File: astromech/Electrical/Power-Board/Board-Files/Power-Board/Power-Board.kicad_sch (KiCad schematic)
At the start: 20 parts

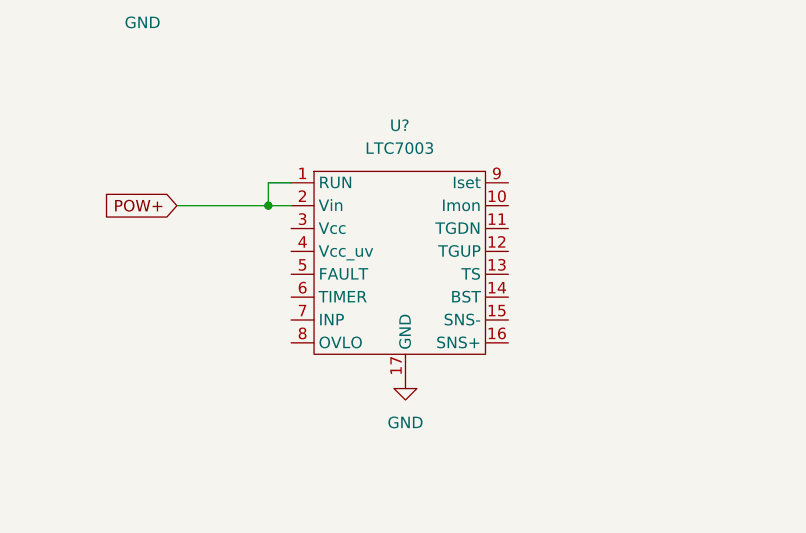
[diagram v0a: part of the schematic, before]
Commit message: Updated LTC7003 symbol
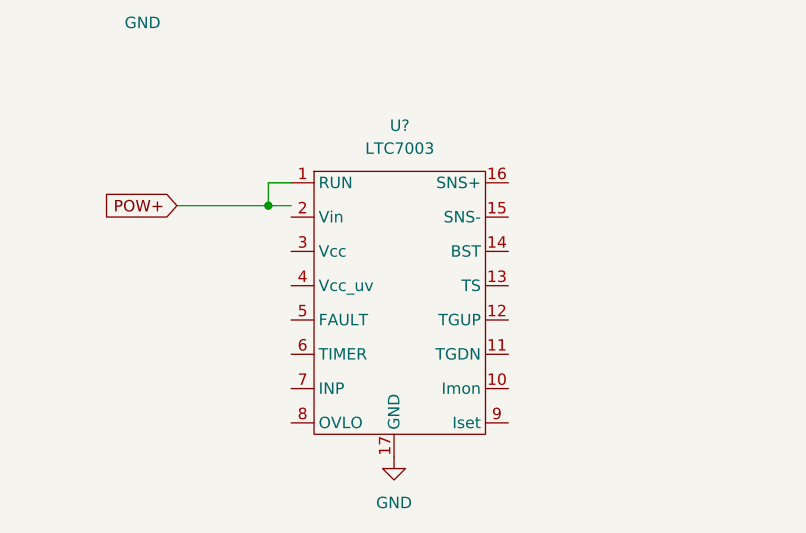
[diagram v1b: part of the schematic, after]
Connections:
- net POW+: no longer U?.2 (Vin)
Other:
- moved on the sheet: U?
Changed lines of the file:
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@@
     (pin "1")
   )
-  (symbol (lib_id "power:GND") (at 115.57 143.51 0) (unit 1)
-    (in_bom yes) (on_board yes) (fields_autoplaced)
-    (property "Reference" "#PWR?" (id 0) (at 115.57 149.86 0)
-      (effects (font (size 1.27 1.27)) hide)
-    )
-    (property "Value" "GND" (id 1) (at 115.57 148.59 0))
-    (property "Footprint" "" (id 2) (at 115.57 143.51 0)
-      (effects (font (size 1.27 1.27)) hide)
-    )
-    (property "Datasheet" "" (id 3) (at 115.57 143.51 0)
+  (symbol (lib_id "power:GND") (at 114.3 152.4 0) (unit 1)
+    (in_bom yes) (on_board yes) (fields_autoplaced)
+    (property "Reference" "#PWR?" (id 0) (at 114.3 158.75 0)
+      (effects (font (size 1.27 1.27)) hide)
+    )
+    (property "Value" "GND" (id 1) (at 114.3 157.48 0))
+    (property "Footprint" "" (id 2) (at 114.3 152.4 0)
+      (effects (font (size 1.27 1.27)) hide)
+    )
+    (property "Datasheet" "" (id 3) (at 114.3 152.4 0)
       (effects (font (size 1.27 1.27)) hide)
     )
@@
       (effects (font (size 1.27 1.27)) hide)
     )
-    (property "Datasheet" "" (id 3) (at 107.95 127 0)
-      (effects (font (size 1.27 1.27)) hide)
-    )
+    (property "Datasheet" "" (id 3) (at 107.95 129.54 0)
+      (effects (font (size 1.27 1.27)) hide)
+    )

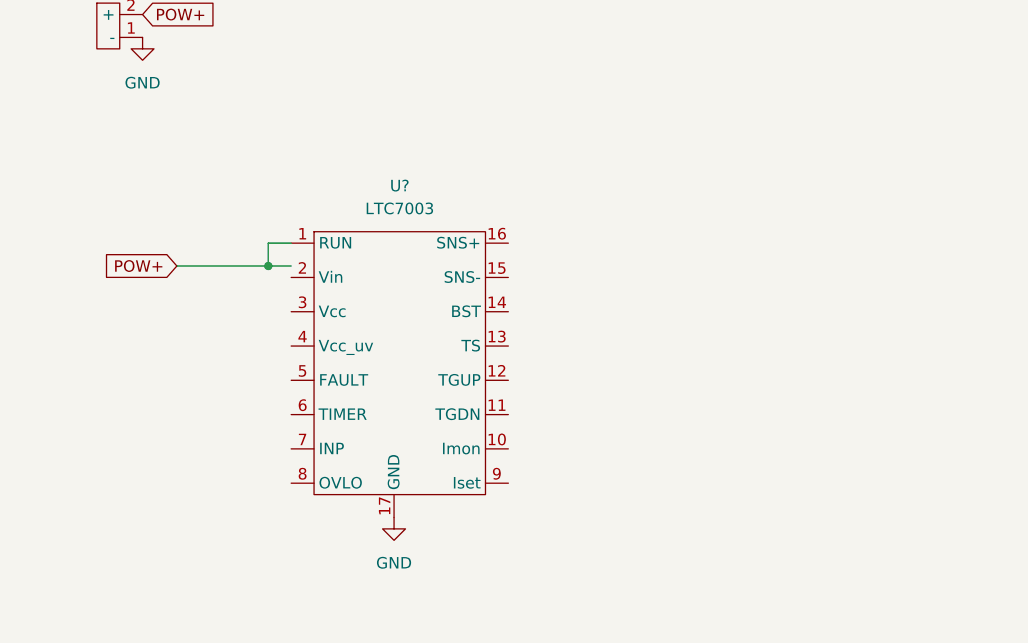
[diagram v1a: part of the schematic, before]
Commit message: added main switch LTC7003
Generic symbols used. Not many symbols have associated footprints
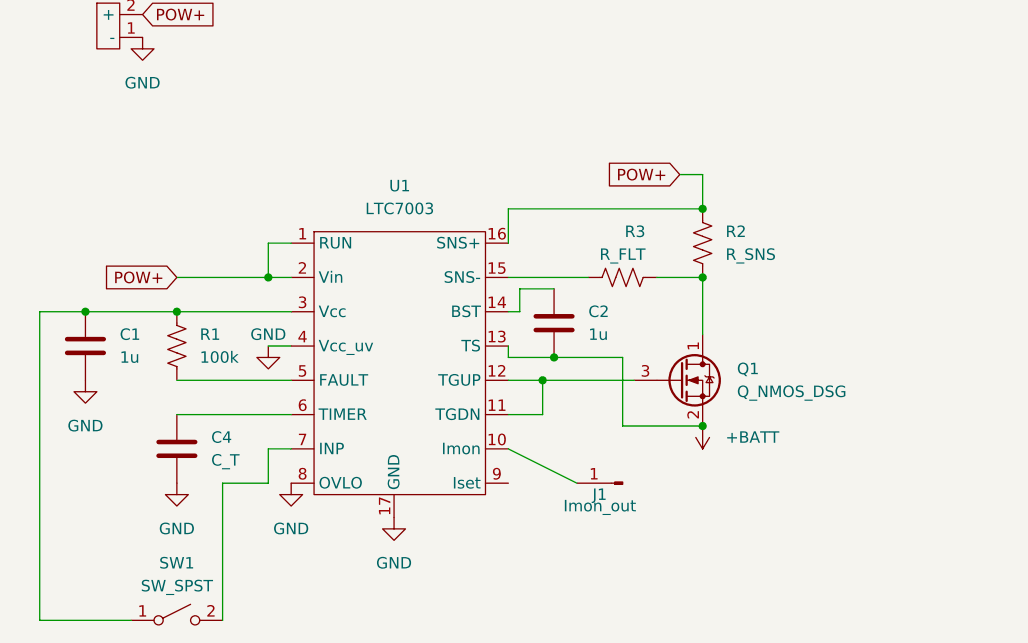
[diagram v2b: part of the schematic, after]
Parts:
- added C1, C2: 1u, symbol Device:C
- added C4: C_T, symbol Device:C
- added J1: Imon_out, symbol Connector:Conn_01x01_Male
- added Q1: Q_NMOS_DSG, symbol Device:Q_NMOS_DSG
- added R1: 100k, symbol Device:R_US
- added R2: R_SNS, symbol Device:R_US
- added R3: R_FLT, symbol Device:R_US
- added SW1: SW_SPST, symbol Switch:SW_SPST
- gave numbers to parts that had none: 1
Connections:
- net +BATT: now also U1.13 (TS), C2.2, Q1.2 (S)
- net GND: now also U1.4 (Vcc_uv), U1.8 (OVLO), C1.2, C4.2
- net POW+: now also U1.16 (SNS+), U1.2 (Vin), R2.1
- net at U1.10 (Imon): now also J1.1 (Pin_1)
- net at U1.11 (TGDN): now also U1.12 (TGUP), Q1.3 (G)
- net at U1.14 (BST): now also C2.1
- net at U1.15 (SNS-): now also R3.1
- net at U1.3 (Vcc): now also C1.1, R1.1, SW1.1 (A)
- net at U1.5 (FAULT): now also R1.2
- net at U1.6 (TIMER): now also C4.1
- net at U1.7 (INP): now also SW1.2 (B)
- new net: Q1.1 (D), R2.2, R3.2

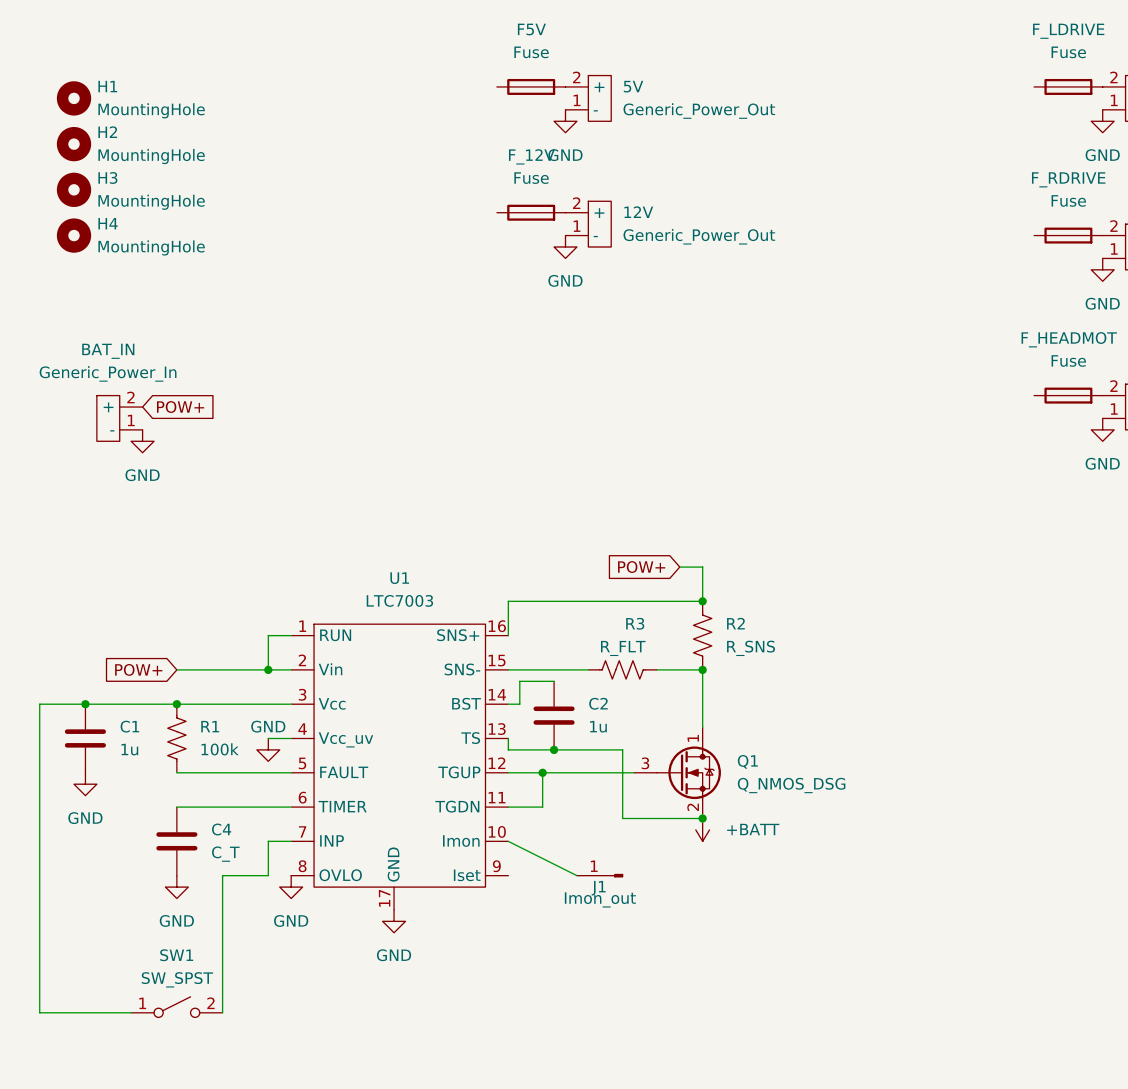
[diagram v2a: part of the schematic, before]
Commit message: Added 5v Regulator
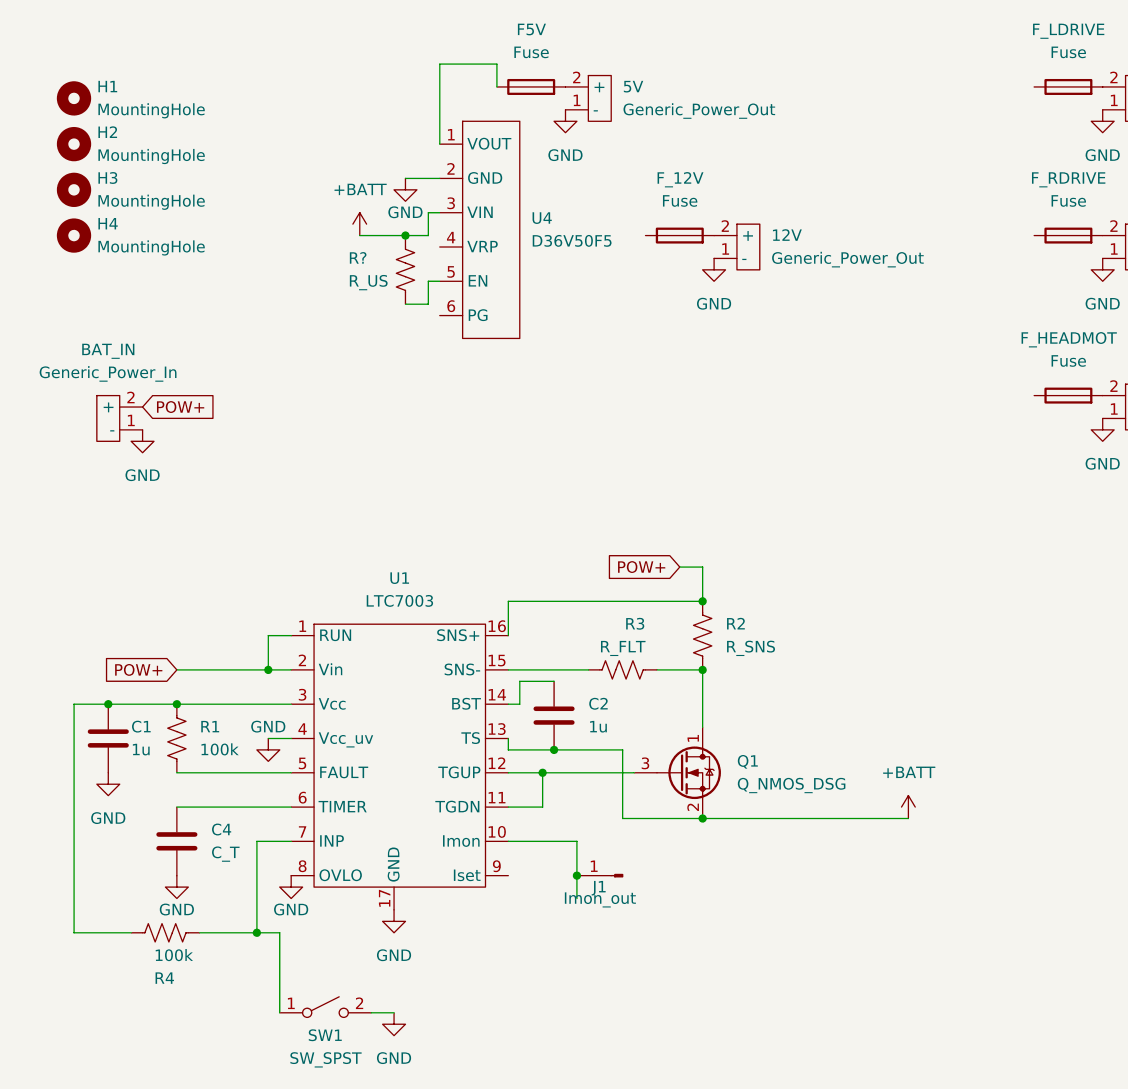
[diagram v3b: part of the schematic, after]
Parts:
- added R4: 100k, symbol Device:R_US
- added R?: R_US, symbol Device:R_US
- added U4: D36V50F5, astromech-footprints:D36V50F5, symbol astromech-power-board:D36V50F5
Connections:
- net +BATT: now also R?.1, U4.3 (VIN)
- net GND: now also SW1.2 (B), U4.2 (GND)
- net at C1.1, R1.1, U1.3 (Vcc): now also R4.2; no longer SW1.1 (A)
- net at U1.7 (INP): now also SW1.1 (A), R4.1; no longer SW1.2 (B)
- net at F5V.1: now also U4.1 (VOUT)
- new net: R?.2, U4.5 (EN)
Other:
- moved on the sheet: 12V, C1, F_12V, SW1

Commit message: various circuit updates
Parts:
- added C4, C5: 1u, symbol Device:C
- added C6: C_T, symbol Device:C
- added J?: Imon_out, symbol Connector:Conn_01x01_Male
- added Q2: Q_NMOS_DSG, symbol Device:Q_NMOS_DSG
- added R5: 100k, symbol Device:R_US
- added R6: R_SNS, symbol Device:R_US
- added R7: R_FLT, symbol Device:R_US
- added U2: LTC7003, astromech-footprints:LTC7003, symbol astromech-power-board:LTC7003
- SW1: value SW_SPST -> SW_NC
- renumbered C4 to C3
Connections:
- net +BATT: now also R6.1, U2.1 (RUN), U2.16 (SNS+), U2.2 (Vin)
- net GND: now also C4.2, C6.2, U2.17 (GND), U2.4 (Vcc_uv), U2.8 (OVLO)
- net at F_HEADMOT.1: now also F_LDRIVE.1, F_RDRIVE.1, C5.2, Q2.2 (S), U2.13 (TS)
- new net: C6.1, U2.6 (TIMER)
- new net: C5.1, U2.14 (BST)
- new net: J?.1 (Pin_1), U2.10 (Imon)
- new net: Q2.3 (G), U2.11 (TGDN), U2.12 (TGUP)
- new net: R7.1, U2.15 (SNS-)
- new net: C4.1, R5.1, U2.3 (Vcc)
- new net: R5.2, U2.5 (FAULT)
- new net: Q2.1 (D), R6.2, R7.2
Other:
- moved on the sheet: 12V, C1, C2, C3, F_12V, F_HEADMOT, F_LDRIVE, F_RDRIVE, HEAD_MOT, J1, L_DRIVE, Q1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

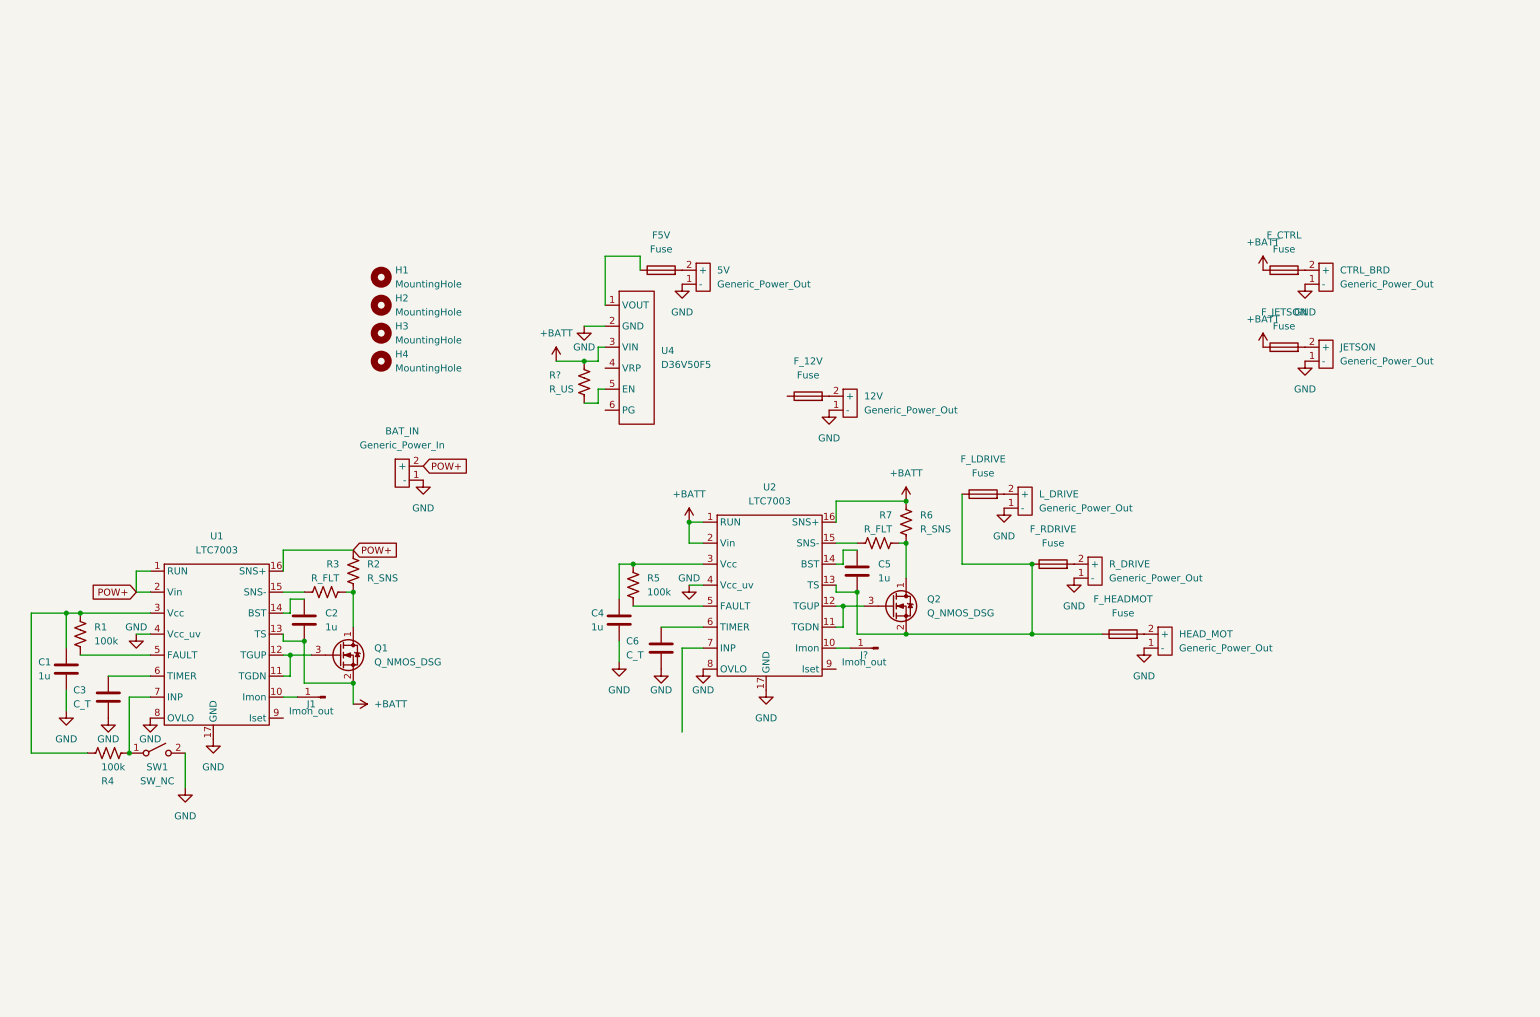
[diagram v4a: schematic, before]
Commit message: added main switch and regulators
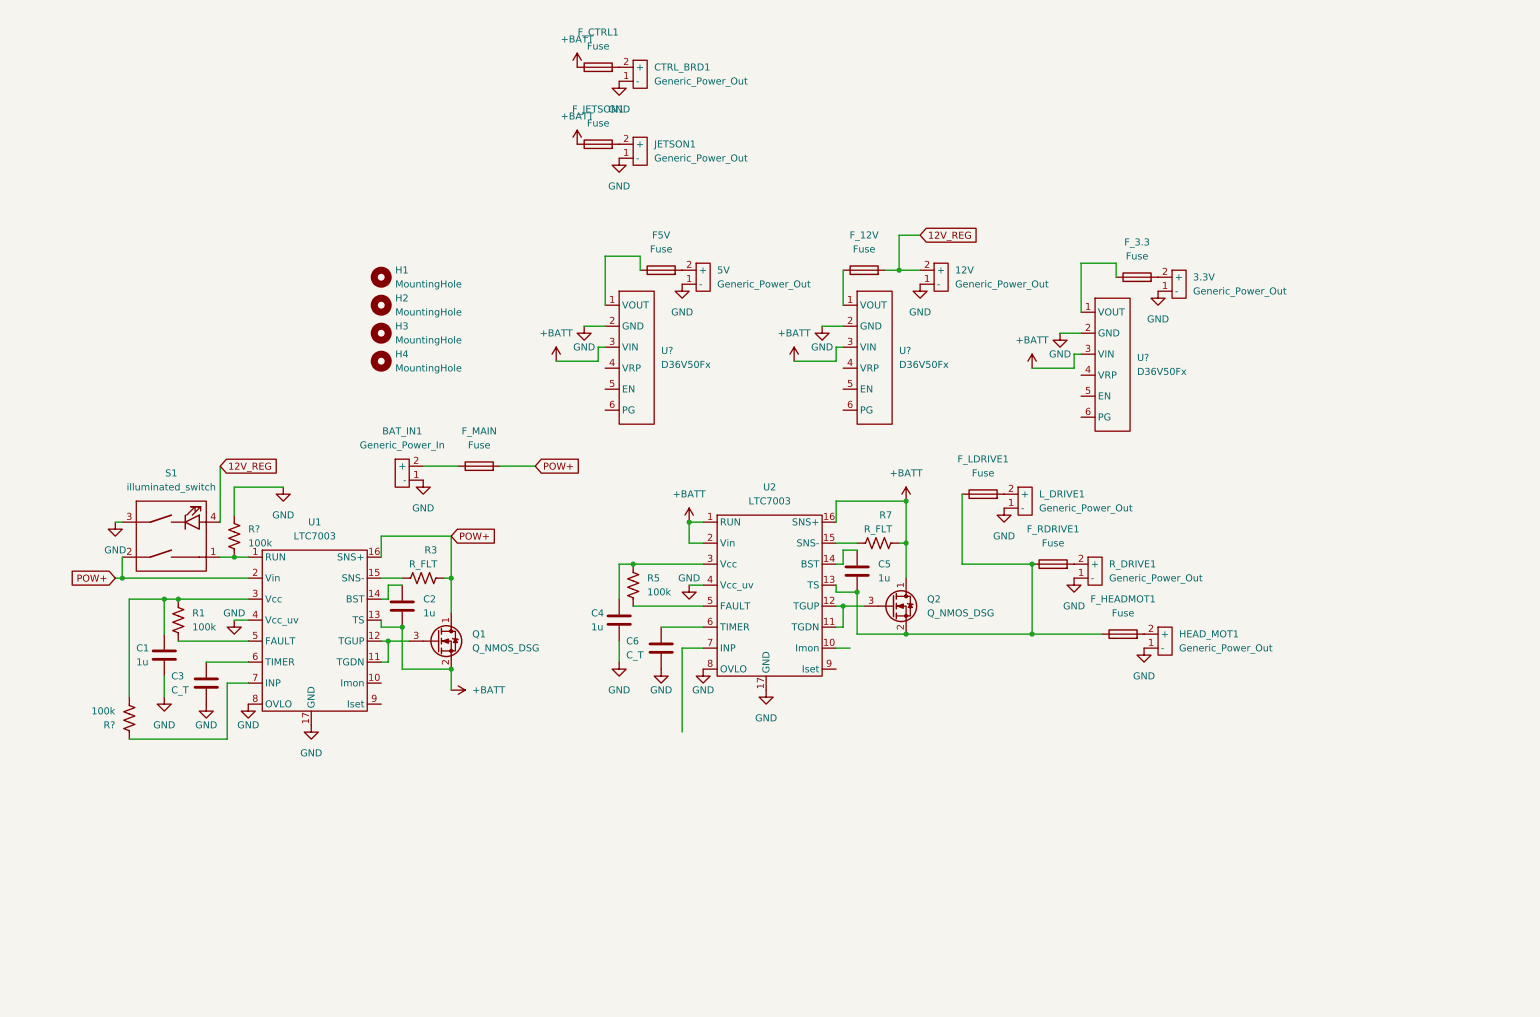
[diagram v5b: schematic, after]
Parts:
- removed J1, J?: Imon_out, symbol Connector:Conn_01x01_Male
- removed R2, R6: R_SNS, symbol Device:R_US
- removed R4: 100k, symbol Device:R_US
- removed R?: R_US, symbol Device:R_US
- removed SW1: SW_NC, symbol Switch:SW_SPST
- removed U4: D36V50F5, astromech-footprints:D36V50F5, symbol astromech-power-board:D36V50F5
- added 3.3V: Generic_Power_Out, symbol astromech-power-board:Generic_Power_Out
- added F_3.3, F_MAIN: Fuse, symbol Device:Fuse
- added R? (x2): 100k, symbol Device:R_US
- added S1: illuminated_switch, symbol astromech-power-board:illuminated_switch
- added U? (x3): D36V50Fx, astromech-footprints:D36V50Fx, symbol astromech-power-board:D36V50Fx
- renumbered BAT_IN to BAT_IN1, CTRL_BRD to CTRL_BRD1, F_CTRL to F_CTRL1, F_HEADMOT to F_HEADMOT1, F_JETSON to F_JETSON1, F_LDRIVE to F_LDRIVE1, F_RDRIVE to F_RDRIVE1, HEAD_MOT to HEAD_MOT1, JETSON to JETSON1, L_DRIVE to L_DRIVE1, R_DRIVE to R_DRIVE1
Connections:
- net +BATT: now also Q2.1 (D), R7.2, U?.3 (VIN), U?.3 (VIN), U?.3 (VIN)
- net GND: now also 3.3V.1 (-), R?.1, S1.3, U?.2 (GND), U?.2 (GND), U?.2 (GND)
- net POW+: now also Q1.1 (D), R3.2, F_MAIN.2, S1.2; no longer BAT_IN1.2 (+), U1.1 (RUN)
- net 12V_REG: now reaches 12V.2 (+), F_12V.2
- net 12V_REG: now also S1.4
- net at C1.1, R1.1, U1.3 (Vcc): now also R?.2
- net at U1.7 (INP): now also R?.1
- net at F5V.1: now also U?.1 (VOUT)
- net at F_12V.1: now also U?.1 (VOUT)
- new net: F_3.3.1, U?.1 (VOUT)
- new net: 3.3V.2 (+), F_3.3.2
- new net: R?.2, S1.1, U1.1 (RUN)
- new net: BAT_IN1.2 (+), F_MAIN.1
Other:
- moved on the sheet: 12V, C1, C2, C3, CTRL_BRD1, F_12V, F_CTRL1, F_JETSON1, JETSON1, Q1, R1, R3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
